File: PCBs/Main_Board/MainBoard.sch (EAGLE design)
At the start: 25 parts

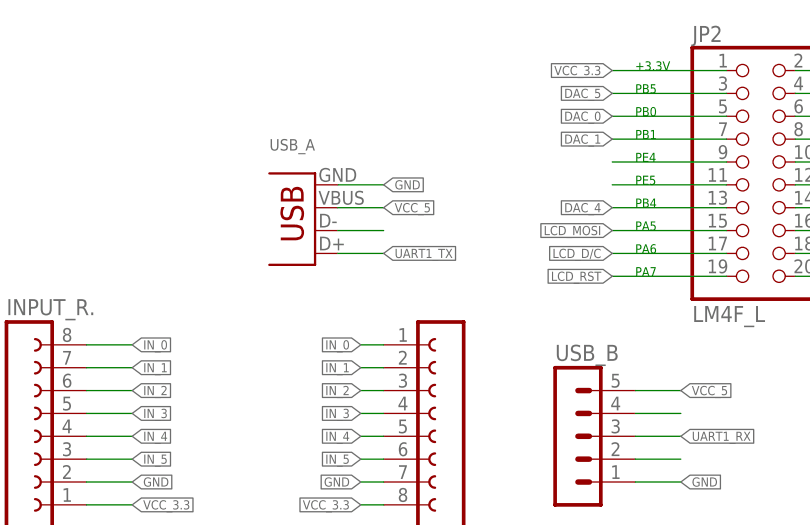
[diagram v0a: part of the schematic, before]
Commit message: Swapped D+/D- pins on the USB A port; misc optimizations
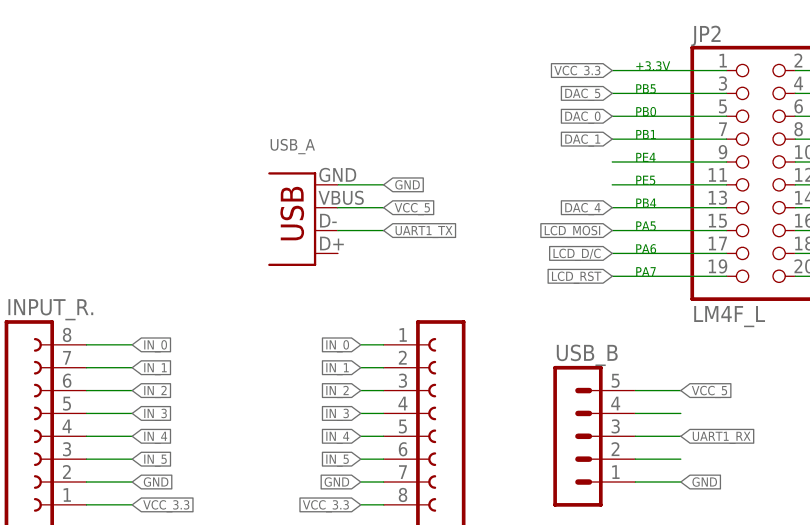
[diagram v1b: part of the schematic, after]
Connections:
- removed net N$67: USB_A.D-
- net UART1_TX: now also USB_A.D-; no longer USB_A.D+
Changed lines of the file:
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@@
 <?xml version="1.0" encoding="utf-8"?>
 <!DOCTYPE eagle SYSTEM "eagle.dtd">
-<eagle version="9.0.0">
+<eagle version="8.3.1">
 <drawing>
 <settings>
@@
 </segment>
 <segment>
-<pinref part="USB_A" gate="G$1" pin="D+"/>
-<wire x1="-5.08" y1="83.82" x2="0" y2="83.82" width="0.1524" layer="91"/>
-<label x="0" y="83.82" size="1.016" layer="95" xref="yes"/>
+<pinref part="USB_A" gate="G$1" pin="D-"/>
+<wire x1="-5.08" y1="86.36" x2="0" y2="86.36" width="0.1524" layer="91"/>
+<label x="0" y="86.36" size="1.016" layer="95" xref="yes"/>
 </segment>
 </net>
@@
 </segment>
 </net>
-<net name="N$67" class="0">
-<segment>
-<pinref part="USB_A" gate="G$1" pin="D-"/>
-<wire x1="-5.08" y1="86.36" x2="0" y2="86.36" width="0.1524" layer="91"/>
-</segment>
-</net>

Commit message: Undid swap
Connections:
- net UART1_TX: now also USB_A.D+; no longer USB_A.D-
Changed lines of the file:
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@@
 </segment>
 <segment>
-<pinref part="USB_A" gate="G$1" pin="D-"/>
-<wire x1="-5.08" y1="86.36" x2="0" y2="86.36" width="0.1524" layer="91"/>
-<label x="0" y="86.36" size="1.016" layer="95" xref="yes"/>
+<pinref part="USB_A" gate="G$1" pin="D+"/>
+<wire x1="-5.08" y1="83.82" x2="0" y2="83.82" width="0.1524" layer="91"/>
+<label x="0" y="83.82" size="1.016" layer="95" xref="yes"/>
 </segment>
 </net>
